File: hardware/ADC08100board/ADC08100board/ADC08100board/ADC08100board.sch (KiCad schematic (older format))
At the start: 18 parts, among them J1 Conn_01x03_Male, J2 Conn_01x03_Male, J3 Conn_02x04_Odd_Even, J4 Conn_01x20_Female

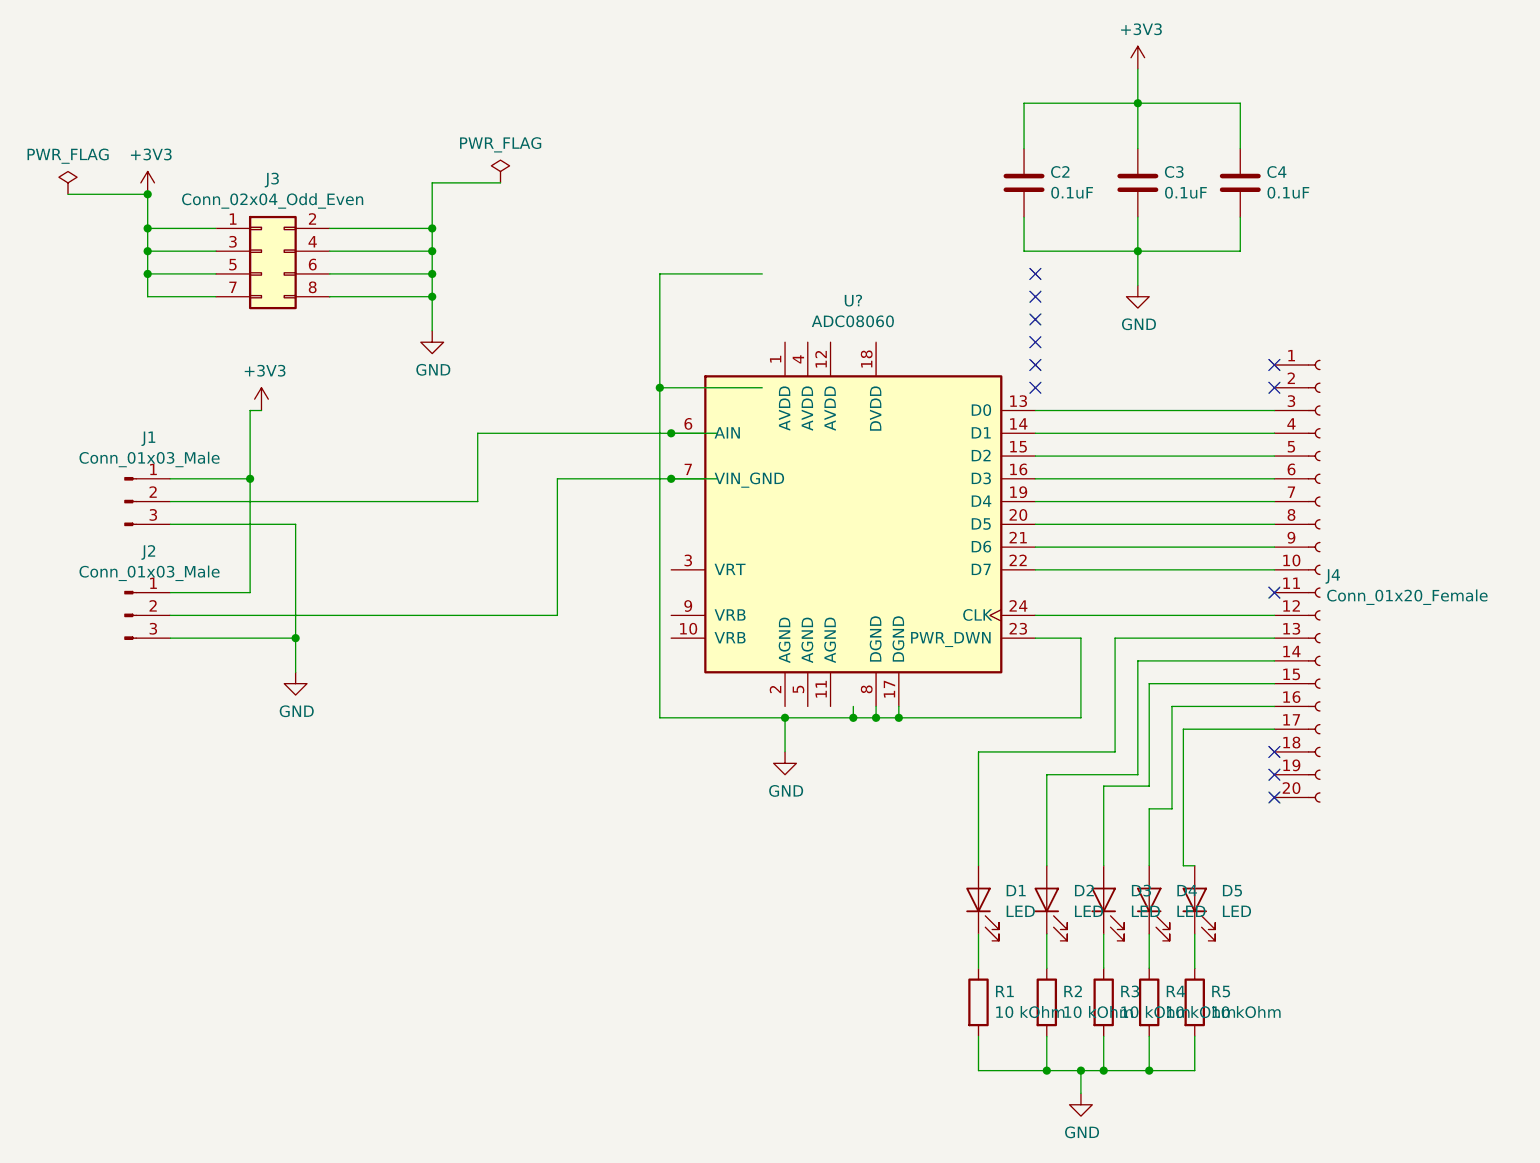
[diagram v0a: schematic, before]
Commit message: THS5641, ADC08100, ADC08060 boards
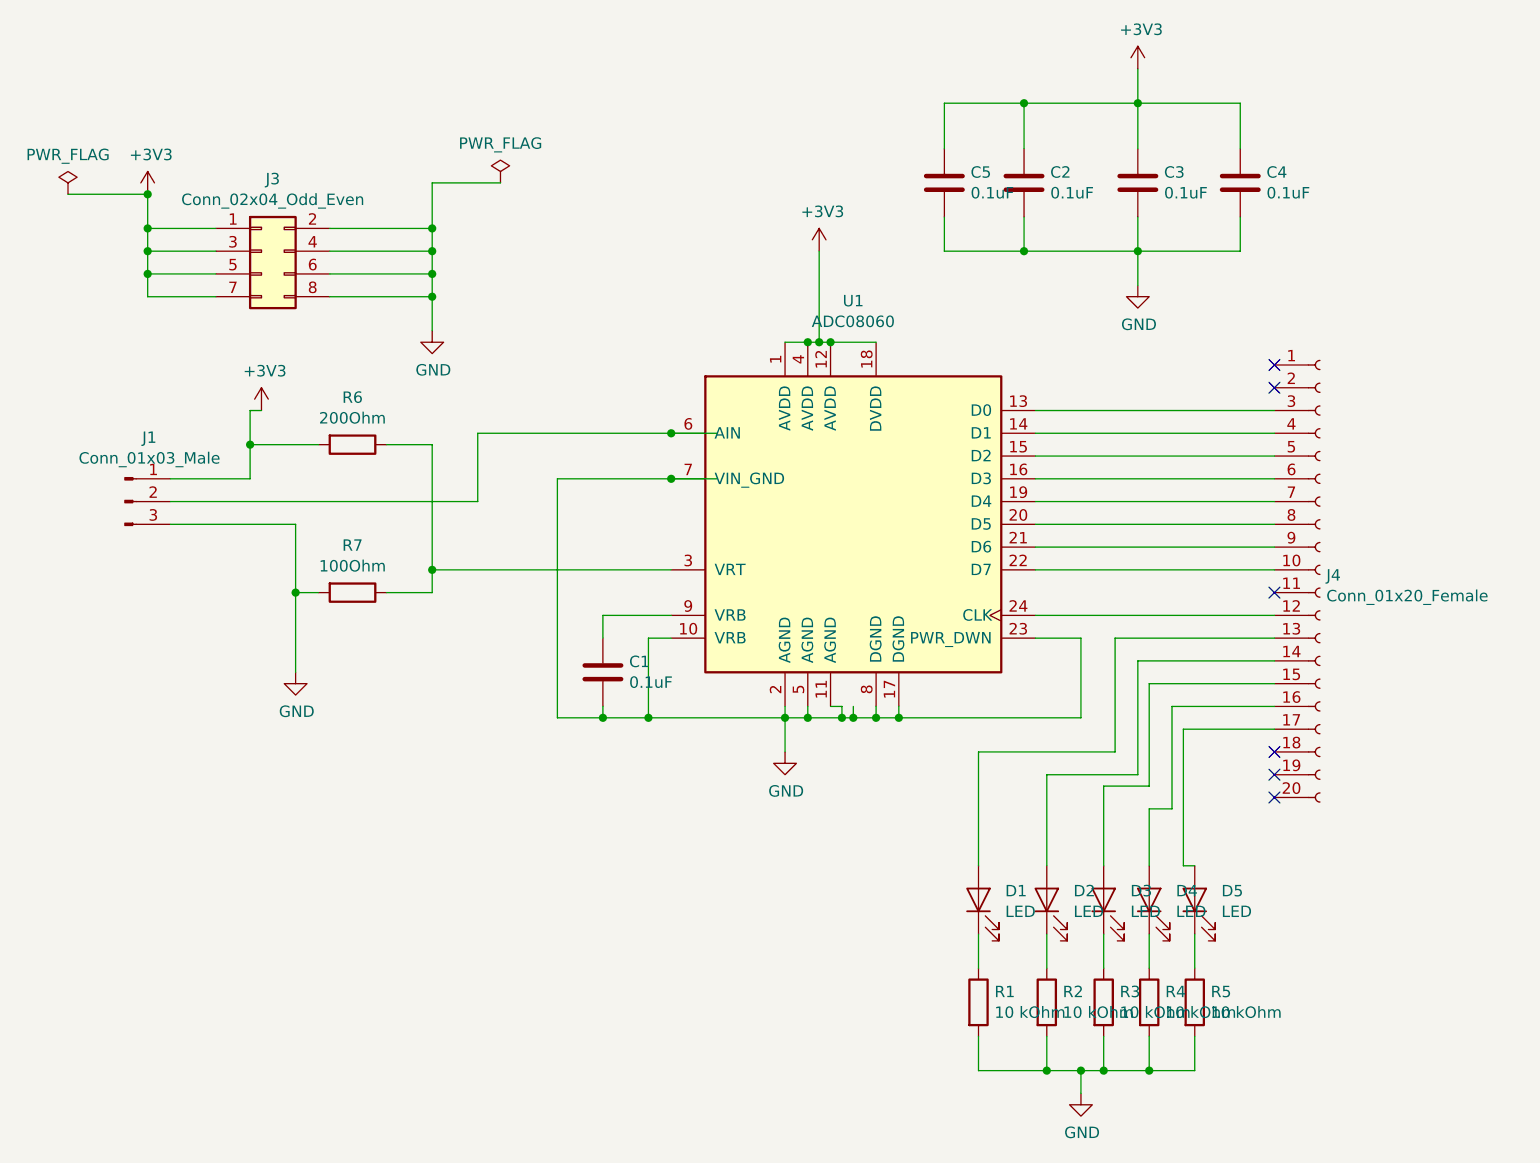
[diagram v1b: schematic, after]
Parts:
- removed J2: Conn_01x03_Male, Connector_PinSocket_2.54mm:PinSocket_1x03_P2.54mm_Vertical, symbol Connector:Conn_01x03_Male
- added C1, C5: 0.1uF, Capacitor_SMD:C_0805_2012Metric, symbol Device:C
- added R6: 200Ohm, Resistor_SMD:R_0805_2012Metric, symbol Device:R
- added R7: 100Ohm, Resistor_SMD:R_0805_2012Metric, symbol Device:R
- U1: renamed from U?; footprint (none) -> Package_SO:TSSOP-24_4.4x7.8mm_P0.65mm
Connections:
- wire segments 107 -> 129
- no-connect marks 12 -> 6
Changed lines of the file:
@@
 $EndComp
-Wire Wire Line
-	4500 3750 5050 3750
 Wire Wire Line
 	5050 3750 5050 3900
 Wire Wire Line
-	5050 3750 5350 3750
+	5050 3750 5150 3750
 Wire Wire Line
 	5550 3750 5550 3700
@@
 $EndComp
 $Comp
-L Connector:Conn_01x03_Male J2
-U 1 1 5DF6DA43
-P 2150 3300
-F 0 "J2" H 2258 3581 50  0000 C CNN
-F 1 "Conn_01x03_Male" H 2258 3490 50  0000 C CNN
-F 2 "Connector_PinSocket_2.54mm:PinSocket_1x03_P2.54mm_Vertical" H 2150 3300 50  0001 C CNN
-F 3 "~" H 2150 3300 50  0001 C CNN
-	1    2150 3300
-	1    0    0    -1
-$EndComp
-$Comp
 L power:GND #PWR03
 U 1 1 5DF70B1C
@@
 Wire Wire Line
 	2350 2900 2900 2900
-Wire Wire Line
-	2900 2900 2900 3400
-Wire Wire Line
-	2350 3400 2900 3400
-Connection ~ 2900 3400
-Wire Wire Line
-	2900 3400 2900 3550
 $Comp
 L power:+3V3 #PWR02
@@
 $EndComp
 Wire Wire Line
-	2350 3200 2700 3200
-Wire Wire Line
-	2700 3200 2700 2700
-Wire Wire Line
 	2700 2400 2750 2400
 Wire Wire Line
 	2350 2700 2700 2700
-Connection ~ 2700 2700
-Wire Wire Line
-	2700 2700 2700 2400
+Wire Wire Line
+	2700 2700 2700 2550
 Wire Wire Line
 	2350 2800 3700 2800
 Wire Wire Line
 	3700 2800 3700 2500
-Wire Wire Line
-	4050 2700 4050 3300
-Wire Wire Line
-	4050 3300 2350 3300
 NoConn ~ 7200 2200
 NoConn ~ 7200 2300
@@
 Wire Wire Line
 	4050 2700 4550 2700
-NoConn ~ 6150 2300
-NoConn ~ 6150 2200
-NoConn ~ 6150 2100
-NoConn ~ 6150 2000
-NoConn ~ 6150 1900
-NoConn ~ 6150 1800
-Wire Wire Line
-	4950 1800 4500 1800
-Wire Wire Line
-	4500 1800 4500 2300
-Wire Wire Line
-	4950 2300 4500 2300
-Connection ~ 4500 2300
-$Comp
-L Analog_ADC:ADC08060 U?
+$Comp
+L Analog_ADC:ADC08060 U1
 U 1 1 5E0E0DA1
 P 5350 2900
-F 0 "U?" H 5350 3881 50  0000 C CNN
+F 0 "U1" H 5350 3881 50  0000 C CNN
 F 1 "ADC08060" H 5350 3790 50  0000 C CNN
-F 2 "" H 5350 2900 50  0001 C CNN
+F 2 "Package_SO:TSSOP-24_4.4x7.8mm_P0.65mm" H 5350 2900 50  0001 C CNN
 F 3 "http://www.ti.com/lit/ds/symlink/adc08060.pdf" H 5350 2900 50  0001 C CNN
 	1    5350 2900
@@
 Wire Wire Line
 	4550 2700 4750 2700
-Wire Wire Line
-	4500 2300 4500 3750
+$Comp
+L Device:C C5
+U 1 1 5E0B376C
+P 5750 1400
+F 0 "C5" H 5865 1446 50  0000 L CNN
+F 1 "0.1uF" H 5865 1355 50  0000 L CNN
+F 2 "Capacitor_SMD:C_0805_2012Metric" H 5788 1250 50  0001 C CNN
+F 3 "~" H 5750 1400 50  0001 C CNN
+	1    5750 1400
+	1    0    0    -1
+$EndComp
+Wire Wire Line
+	5750 1250 5750 1050
+Wire Wire Line
+	6100 1050 5750 1050
+Connection ~ 6100 1050
+Wire Wire Line
+	5750 1550 5750 1700
+Wire Wire Line
+	5750 1700 6100 1700
+Connection ~ 6100 1700
+Wire Wire Line
+	2900 2900 2900 3200
+Wire Wire Line
+	4050 3750 4250 3750
+Wire Wire Line
+	4050 2700 4050 3750
+Wire Wire Line
+	4550 3400 4450 3400
+Wire Wire Line
+	4450 3400 4450 3750
+Connection ~ 4450 3750
+Wire Wire Line
+	4450 3750 5050 3750
+$Comp
+L Device:C C1
+U 1 1 5E0C987D
+P 4250 3550
+F 0 "C1" H 4365 3596 50  0000 L CNN
+F 1 "0.1uF" H 4365 3505 50  0000 L CNN
+F 2 "Capacitor_SMD:C_0805_2012Metric" H 4288 3400 50  0001 C CNN
+F 3 "~" H 4250 3550 50  0001 C CNN
+	1    4250 3550
+	1    0    0    -1
+$EndComp
+Wire Wire Line
+	4550 3300 4250 3300
+Wire Wire Line
+	4250 3300 4250 3400
+Wire Wire Line
+	4250 3700 4250 3750
+Connection ~ 4250 3750
+Wire Wire Line
+	4250 3750 4450 3750
+Wire Wire Line
+	5150 3700 5150 3750
+Connection ~ 5150 3750
+Wire Wire Line
+	5150 3750 5300 3750
+Wire Wire Line
+	5250 3700 5300 3700
+Wire Wire Line
+	5300 3700 5300 3750
+Connection ~ 5300 3750
+Wire Wire Line
+	5300 3750 5350 3750
+$Comp
+L power:+3V3 #PWR06
+U 1 1 5E0E09FB
+P 5200 1700
+F 0 "#PWR06" H 5200 1550 50  0001 C CNN
+F 1 "+3V3" H 5215 1873 50  0000 C CNN
+F 2 "" H 5200 1700 50  0001 C CNN
+F 3 "" H 5200 1700 50  0001 C CNN
+	1    5200 1700
+	1    0    0    -1
+$EndComp
+Wire Wire Line
+	5200 1700 5200 2100
+Wire Wire Line
+	5200 2100 5150 2100
+Connection ~ 5150 2100
+Wire Wire Line
+	5150 2100 5050 2100
+Wire Wire Line
+	5200 2100 5250 2100
+Connection ~ 5200 2100
+Connection ~ 5250 2100
+Wire Wire Line
+	5250 2100 5450 2100
+$Comp
+L Device:R R6
+U 1 1 5E0EC9D5
+P 3150 2550
+F 0 "R6" V 2943 2550 50  0000 C CNN
+F 1 "200Ohm" V 3034 2550 50  0000 C CNN
+F 2 "Resistor_SMD:R_0805_2012Metric" V 3080 2550 50  0001 C CNN
+F 3 "~" H 3150 2550 50  0001 C CNN
+	1    3150 2550
+	0    1    1    0
+$EndComp
+$Comp
+L Device:R R7
+U 1 1 5E0ED2C7
+P 3150 3200
+F 0 "R7" V 2943 3200 50  0000 C CNN
+F 1 "100Ohm" V 3034 3200 50  0000 C CNN
+F 2 "Resistor_SMD:R_0805_2012Metric" V 3080 3200 50  0001 C CNN
+F 3 "~" H 3150 3200 50  0001 C CNN
+	1    3150 3200
+	0    1    1    0
+$EndComp
+Wire Wire Line
+	2700 2550 3000 2550
+Connection ~ 2700 2550
+Wire Wire Line
+	2700 2550 2700 2400
+Wire Wire Line
+	2900 3200 3000 3200
+Connection ~ 2900 3200
+Wire Wire Line
+	2900 3200 2900 3550
+Wire Wire Line
+	3300 2550 3500 2550
+Wire Wire Line
+	3500 2550 3500 3100
+Wire Wire Line
+	3500 3200 3300 3200
+Wire Wire Line
+	4550 3100 3500 3100
+Connection ~ 3500 3100
+Wire Wire Line
+	3500 3100 3500 3200
+Wire Wire Line
+	5050 3700 5050 3750
 $EndSCHEMATC
